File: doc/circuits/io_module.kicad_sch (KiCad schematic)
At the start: 14 parts, among them SW1 SW_MEC_5G, SW3 SW_MEC_5G, U1 RC1602A-GHW-ESX, U2 74LS04, U3 74HC595, U4 ATmega328P-P, U5 74AUC1G74, U6 74AUC1G74, U7 74LS02, Y1 Crystal

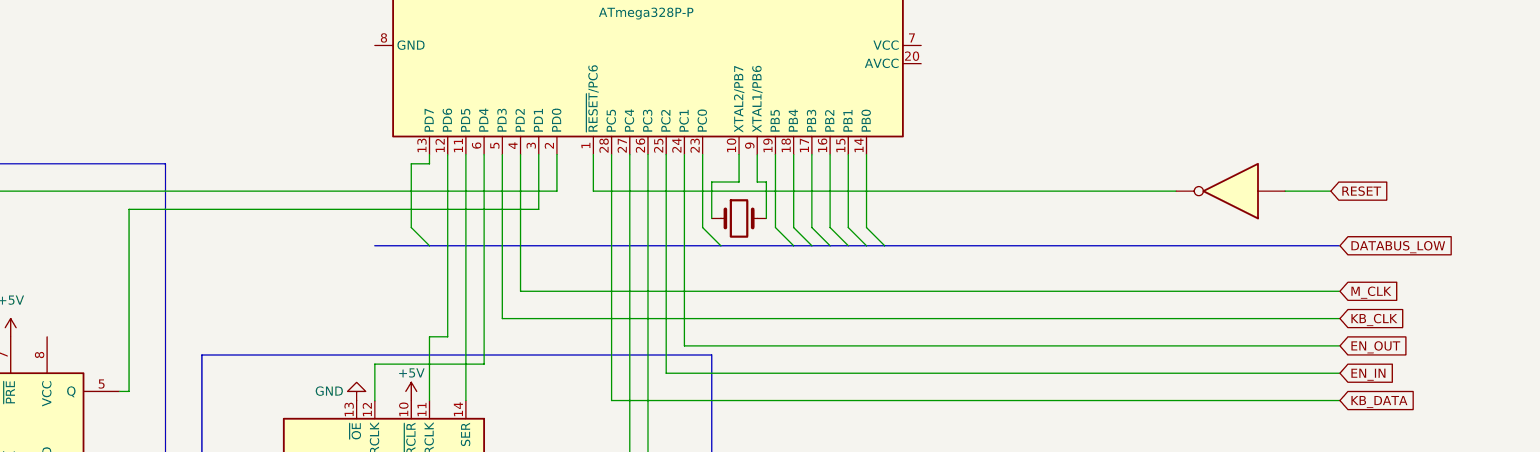
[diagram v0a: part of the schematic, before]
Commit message: improved IO, documentation updated
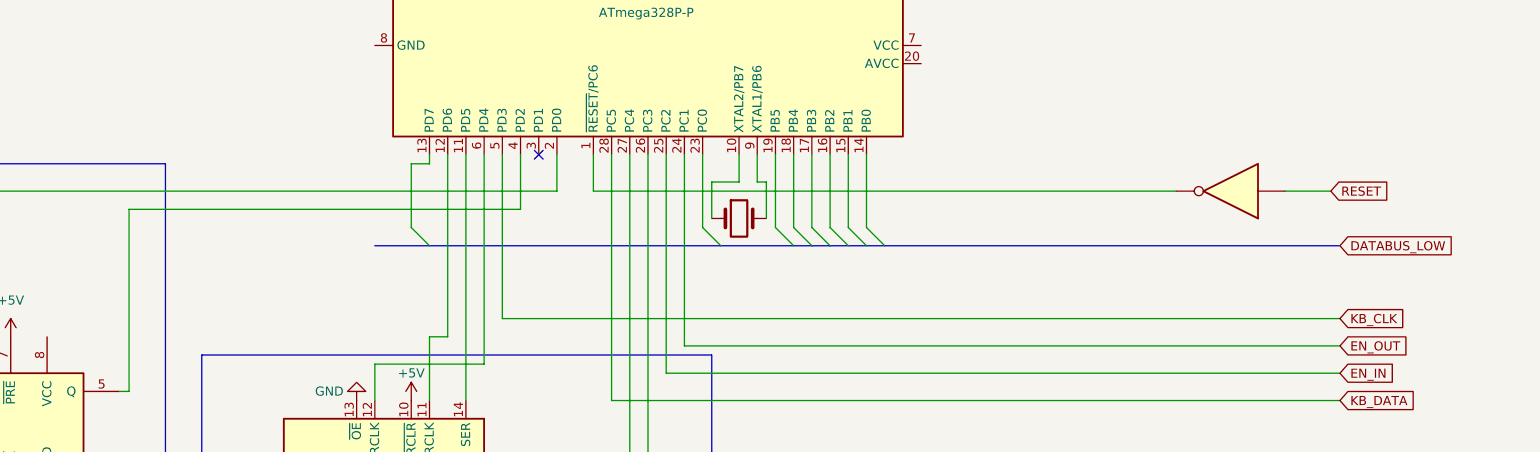
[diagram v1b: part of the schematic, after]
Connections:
- net M_CLK: no longer U4.4 (PD2)
- net at U4.3 (PD1): no longer U6.5 (Q)
- new net: U4.4 (PD2), U6.5 (Q)
- no-connect marks 9 -> 10
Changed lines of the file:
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@@
+	)
+	(no_connect
+		(at 149.86 53.34)
 	)
 	(no_connect
@@
 	(wire
 		(pts
-			(xy 149.86 53.34) (xy 149.86 60.96)
-		)
-		(stroke
-			(width 0)
-			(type default)
-		)
-	)
-	(wire
-		(pts
 			(xy 170.18 80.01) (xy 170.18 53.34)
 		)
@@
 	(wire
 		(pts
-			(xy 147.32 53.34) (xy 147.32 72.39)
-		)
-		(stroke
-			(width 0)
-			(type default)
-		)
-	)
-	(wire
-		(pts
 			(xy 121.92 115.57) (xy 110.49 115.57)
 		)
@@
 	(wire
 		(pts
-			(xy 261.62 72.39) (xy 147.32 72.39)
-		)
-		(stroke
-			(width 0)
-			(type default)
-		)
-	)
-	(wire
-		(pts
 			(xy 152.4 53.34) (xy 152.4 58.42)
 		)
@@
 	(wire
 		(pts
-			(xy 149.86 60.96) (xy 92.71 60.96)
-		)
-		(stroke
-			(width 0)
-			(type default)
-		)
-	)
-	(wire
-		(pts
 			(xy 59.69 86.36) (xy 66.04 86.36)
 		)
@@
 		)
 	)
+	(wire
+		(pts
+			(xy 147.32 60.96) (xy 92.71 60.96)
+		)
+		(stroke
+			(width 0)
+			(type default)
+		)
+	)
 	(bus
 		(pts
@@
 		(pts
 			(xy 44.45 104.14) (xy 44.45 109.22)
+		)
+		(stroke
+			(width 0)
+			(type default)
+		)
+	)
+	(wire
+		(pts
+			(xy 147.32 53.34) (xy 147.32 60.96)
 		)
 		(stroke
@@
 				(hide yes)
 			)
-		)
-	)
-	(global_label "M_CLK"
-		(shape input)
-		(at 261.62 72.39 0)
-		(fields_autoplaced yes)
-		(effects
-			(font
-				(size 1.27 1.27)
-			)
-			(justify left)
-		)
-		(property "Intersheetrefs" "${INTERSHEET_REFS}"
-			(at 270.5923 72.39 0)
-			(effects
-				(font
-					(size 1.27 1.27)
-				)
-				(justify left)
-				(hide yes)
-			)

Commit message: documentation
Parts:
- removed U7: 74LS02, symbol 74xx:74LS02
- added U10, U11, U8, U9: 74LS02, symbol 74xx:74LS02
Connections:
- net CLR_K: now also U9.2, U9.3
- net M_CLK: now also U8.2, U8.3
- net RESET: now also U11.2
- net at U5.6 (~{CLR}), U6.6 (~{CLR}): now also U11.1
- new net: U10.1, U11.3
- new net: U10.3, U8.1
- new net: U10.2, U9.1
